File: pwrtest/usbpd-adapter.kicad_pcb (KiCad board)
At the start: 2 copper layers, 61.2 x 45.5 mm, 49 parts, among them J1 Conn_01x04, J2 Conn_01x04, J3 USB_C_Receptacle_USB2.0_16P, J5 Screw_Terminal_01x03, Q1 AO3400A, U1 AP63205WU, U2 L7812, U3 IP2721, U4 TPS5430DDA, U5 L7905

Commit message: adding undervoltage detection circuits
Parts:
- added D10: LED, Diode_SMD:D_0603_1608Metric_Pad1.05x0.95mm_HandSolder, F.Cu at (114.0, 39.2)
- added D11: LED, Diode_SMD:D_0603_1608Metric_Pad1.05x0.95mm_HandSolder, F.Cu at (114.0, 41.8)
- added D12: LED, Diode_SMD:D_0603_1608Metric_Pad1.05x0.95mm_HandSolder, F.Cu at (114.0, 44.4)
- added D8: LED, Diode_SMD:D_0603_1608Metric_Pad1.05x0.95mm_HandSolder, F.Cu at (114.0, 34.0)
- added D9: LED, Diode_SMD:D_0603_1608Metric_Pad1.05x0.95mm_HandSolder, F.Cu at (114.0, 36.6)
- added Q2: BC847, Package_TO_SOT_SMD:SOT-23, F.Cu at (91.4, 34.9)
- added Q3: BC847, Package_TO_SOT_SMD:SOT-23, F.Cu at (91.4, 39.4)
- added Q4: BC847, Package_TO_SOT_SMD:SOT-23, F.Cu at (91.4, 43.8)
- added Q5: BC847, Package_TO_SOT_SMD:SOT-23, F.Cu at (91.4, 48.3)
- added Q6: BC857, Package_TO_SOT_SMD:SOT-23, F.Cu at (91.4, 52.7)
- added R11: 36k, Resistor_SMD:R_0603_1608Metric_Pad0.98x0.95mm_HandSolder, F.Cu at (100.9, 34.0)
- added R14: 10k, Resistor_SMD:R_0603_1608Metric_Pad0.98x0.95mm_HandSolder, F.Cu at (100.9, 36.5)
- added R15: 10k, Resistor_SMD:R_0603_1608Metric_Pad0.98x0.95mm_HandSolder, F.Cu at (100.9, 39.0)
- added R16: 560, Resistor_SMD:R_0603_1608Metric_Pad0.98x0.95mm_HandSolder, F.Cu at (100.9, 41.5)
- added R17: 47k, Resistor_SMD:R_0603_1608Metric_Pad0.98x0.95mm_HandSolder, F.Cu at (100.9, 44.0)
- added R18: 10k, Resistor_SMD:R_0603_1608Metric_Pad0.98x0.95mm_HandSolder, F.Cu at (100.9, 46.5)
- added R19: 10k, Resistor_SMD:R_0603_1608Metric_Pad0.98x0.95mm_HandSolder, F.Cu at (100.9, 49.0)
- added R20: 560, Resistor_SMD:R_0603_1608Metric_Pad0.98x0.95mm_HandSolder, F.Cu at (100.9, 51.5)
- added R21: 8.2k, Resistor_SMD:R_0603_1608Metric_Pad0.98x0.95mm_HandSolder, F.Cu at (105.2, 34.0)
- added R22: 10k, Resistor_SMD:R_0603_1608Metric_Pad0.98x0.95mm_HandSolder, F.Cu at (105.2, 36.5)
- added R23: 10k, Resistor_SMD:R_0603_1608Metric_Pad0.98x0.95mm_HandSolder, F.Cu at (105.2, 39.0)
- added R24: 560, Resistor_SMD:R_0603_1608Metric_Pad0.98x0.95mm_HandSolder, F.Cu at (105.2, 41.5)
- added R25: 36k, Resistor_SMD:R_0603_1608Metric_Pad0.98x0.95mm_HandSolder, F.Cu at (105.2, 44.0)
- added R26: 10k, Resistor_SMD:R_0603_1608Metric_Pad0.98x0.95mm_HandSolder, F.Cu at (105.2, 46.5)
- added R27: 10k, Resistor_SMD:R_0603_1608Metric_Pad0.98x0.95mm_HandSolder, F.Cu at (105.2, 49.0)
- added R28: 560, Resistor_SMD:R_0603_1608Metric_Pad0.98x0.95mm_HandSolder, F.Cu at (105.2, 51.5)
- added R29: 10k, Resistor_SMD:R_0603_1608Metric_Pad0.98x0.95mm_HandSolder, F.Cu at (109.6, 34.0)
- added R30: 8.2k, Resistor_SMD:R_0603_1608Metric_Pad0.98x0.95mm_HandSolder, F.Cu at (109.6, 36.5)
- added R31: 10k, Resistor_SMD:R_0603_1608Metric_Pad0.98x0.95mm_HandSolder, F.Cu at (109.6, 39.0)
- added R32: 560, Resistor_SMD:R_0603_1608Metric_Pad0.98x0.95mm_HandSolder, F.Cu at (109.6, 41.5)
- added R33: 10k, Resistor_SMD:R_0603_1608Metric_Pad0.98x0.95mm_HandSolder, F.Cu at (109.6, 44.0)
- added R34: 10k, Resistor_SMD:R_0603_1608Metric_Pad0.98x0.95mm_HandSolder, F.Cu at (109.6, 46.5)
- added U10: TL431, Package_TO_SOT_SMD:SOT-23, F.Cu at (96.3, 52.7)
- added U6: TL431DBZ, Package_TO_SOT_SMD:SOT-23, F.Cu at (96.3, 34.9)
- added U7: TL431DBZ, Package_TO_SOT_SMD:SOT-23, F.Cu at (96.3, 39.4)
- added U8: TL431DBZ, Package_TO_SOT_SMD:SOT-23, F.Cu at (96.3, 43.8)
- added U9: TL431, Package_TO_SOT_SMD:SOT-23, F.Cu at (96.3, 48.3)
- R12: value 620 -> 390
- R13: value 2k -> 1.8k

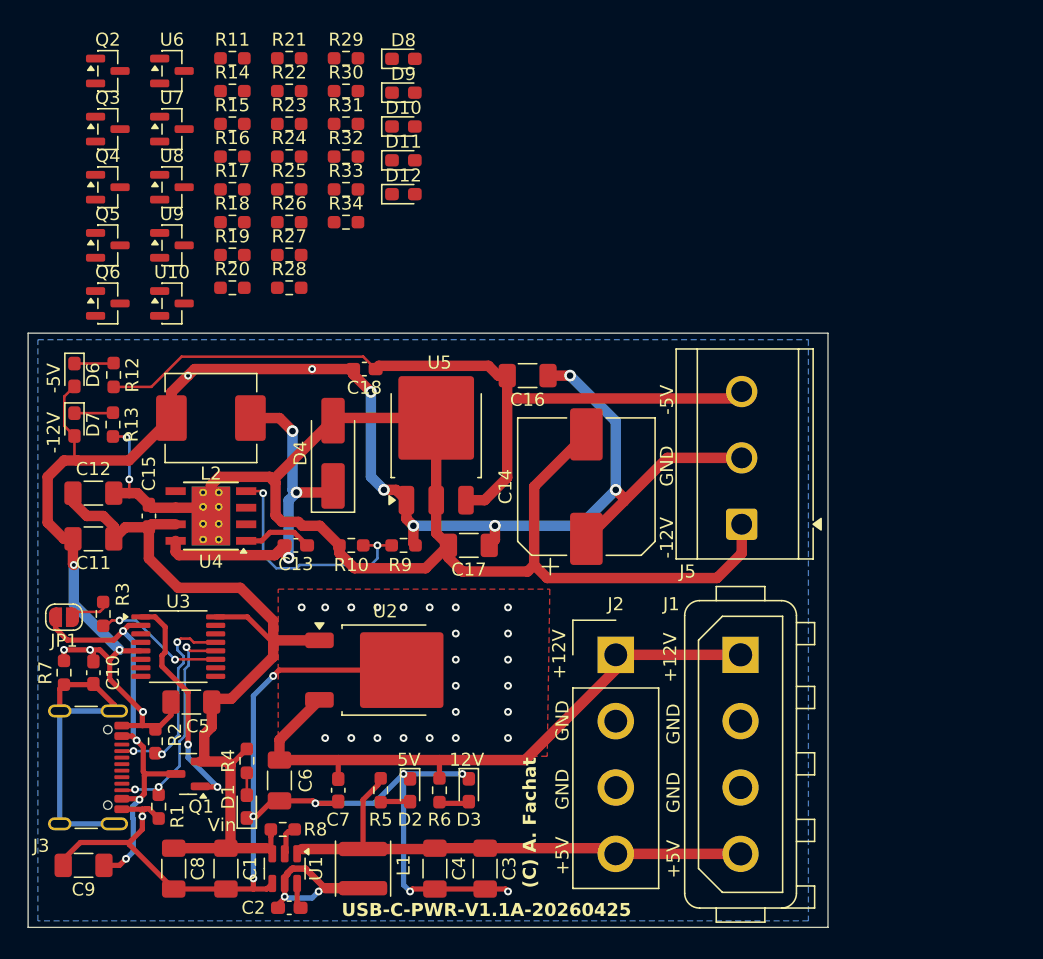
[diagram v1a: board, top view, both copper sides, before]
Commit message: new pwr adapter layout
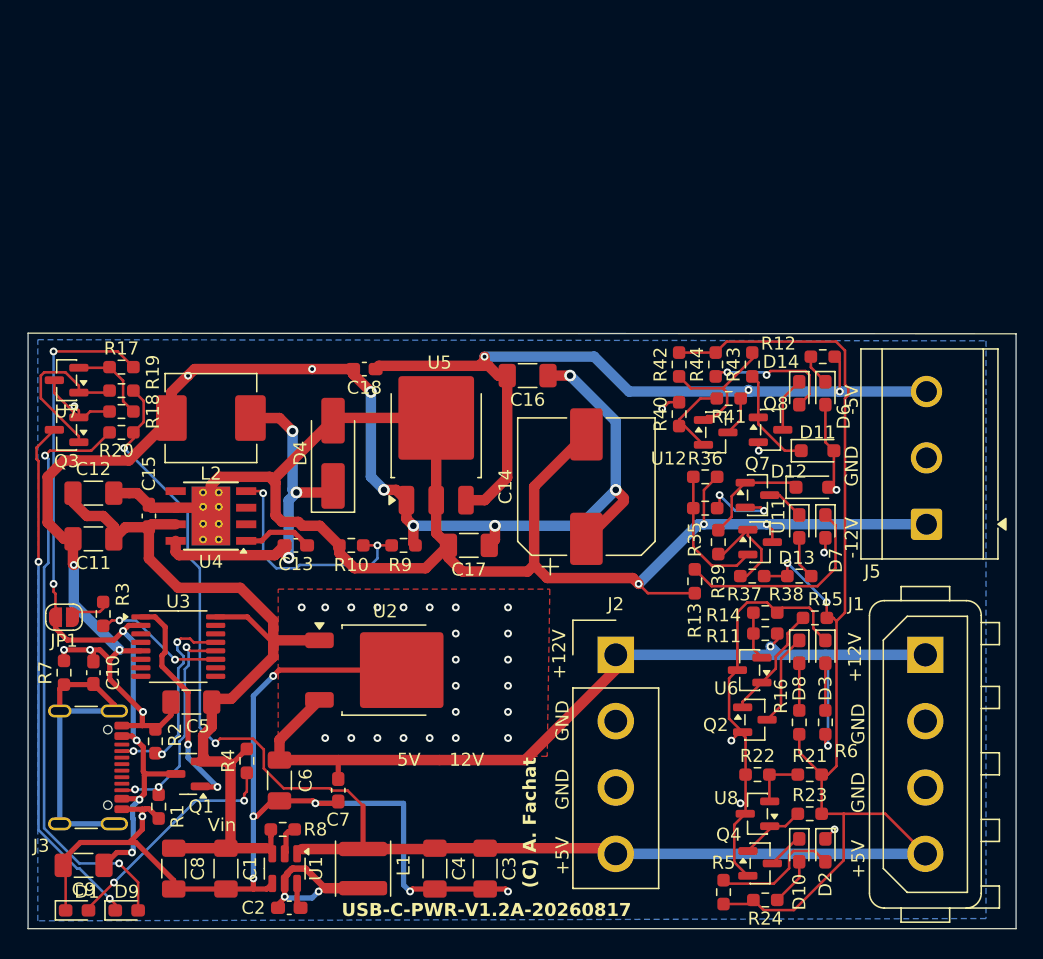
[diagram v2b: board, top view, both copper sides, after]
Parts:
- removed Q5: BC847, Package_TO_SOT_SMD:SOT-23
- removed Q6: BC857, Package_TO_SOT_SMD:SOT-23
- removed R25: 36k, Resistor_SMD:R_0603_1608Metric_Pad0.98x0.95mm_HandSolder
- removed R26, R27, R29, R31, R33, R34: 10k, Resistor_SMD:R_0603_1608Metric_Pad0.98x0.95mm_HandSolder
- removed R28, R32: 560, Resistor_SMD:R_0603_1608Metric_Pad0.98x0.95mm_HandSolder
- removed R30: 8.2k, Resistor_SMD:R_0603_1608Metric_Pad0.98x0.95mm_HandSolder
- removed U10, U9: TL431, Package_TO_SOT_SMD:SOT-23
- added D13: LED, Diode_SMD:D_0603_1608Metric_Pad1.05x0.95mm_HandSolder, F.Cu at (144.3, 69.8)
- added D14: LED, Diode_SMD:D_0603_1608Metric_Pad1.05x0.95mm_HandSolder, F.Cu at (144.3, 59.6)
- added Q7: BC847, Package_TO_SOT_SMD:SOT-23, F.Cu at (141.1, 67.4)
- added Q8: BC847, Package_TO_SOT_SMD:SOT-23, F.Cu at (142.1, 62.4)
- added R35: 36k, Resistor_SMD:R_0603_1608Metric_Pad0.98x0.95mm_HandSolder, F.Cu at (137.1, 68.4)
- added R36: 10k, Resistor_SMD:R_0603_1608Metric_Pad0.98x0.95mm_HandSolder, F.Cu at (137.1, 66.0)
- added R37: 2.2k, Resistor_SMD:R_0603_1608Metric_Pad0.98x0.95mm_HandSolder, F.Cu at (140.7, 73.6)
- added R38: 560, Resistor_SMD:R_0603_1608Metric_Pad0.98x0.95mm_HandSolder, F.Cu at (144.3, 73.6)
- added R39: 10k, Resistor_SMD:R_0603_1608Metric_Pad0.98x0.95mm_HandSolder, F.Cu at (138.1, 71.0)
- added R40: 8.6k, Resistor_SMD:R_0603_1608Metric_Pad0.98x0.95mm_HandSolder, F.Cu at (135.1, 61.2)
- added R41: 10k, Resistor_SMD:R_0603_1608Metric_Pad0.98x0.95mm_HandSolder, F.Cu at (138.9, 60.0)
- added R42: 2.2k, Resistor_SMD:R_0603_1608Metric_Pad0.98x0.95mm_HandSolder, F.Cu at (135.1, 57.4)
- added R43: 10k, Resistor_SMD:R_0603_1608Metric_Pad0.98x0.95mm_HandSolder, F.Cu at (140.7, 57.4)
- added R44: 560, Resistor_SMD:R_0603_1608Metric_Pad0.98x0.95mm_HandSolder, F.Cu at (137.9, 57.4)
- added U11: TL431, Package_TO_SOT_SMD:SOT-23, F.Cu at (141.3, 71.0)
- added U12: TL431, Package_TO_SOT_SMD:SOT-23, F.Cu at (137.9, 62.6)
- D11, D12: value LED -> 1N4148; footprint Diode_SMD:D_0603_1608Metric_Pad1.05x0.95mm_HandSolder -> Diode_SMD:D_SOD-323_HandSoldering
- moved Q4 71.9 mm to (141.3, 95.6)
- moved Q2 70.2 mm to (140.9, 84.6)
- moved R21 67.8 mm to (145.1, 88.8)
- moved R24 67.6 mm to (141.7, 98.4), turned to 180 degrees
- moved R23 66.2 mm to (145.1, 91.8)
- moved D9 66.1 mm to (92.8, 99.2)
- moved U8 65.7 mm to (141.1, 91.8), turned to 180 degrees
- moved U6 63.7 mm to (140.5, 80.8), turned to 180 degrees
- moved R22 63.4 mm to (141.1, 88.8)
- moved D10 63.2 mm to (144.3, 94.6), turned to -90 degrees
- moved R16 61.3 mm to (144.3, 84.8), turned to -90 degrees
- moved R11 60.0 mm to (141.7, 78.0)
- moved R15 58.5 mm to (145.5, 76.8)
- moved D7 58.0 mm to (146.3, 69.8)
- moved D6 57.5 mm to (146.3, 59.6)
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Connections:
- D11 pad 1: -5V -> Net-(D11-K)
- D11 pad 2: Net-(D11-A) -> GND
- D12 pad 2: Net-(D12-A) -> GND
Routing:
- net 5V: track 40.3 -> 183.9 mm, vias 0 -> 4
- net Net-(D9-A): track 0.00 -> 45.5 mm, vias 0 -> 2
- net Net-(D9-K): track 0.00 -> 40.0 mm, vias 0 -> 2
- net GND: track 221.5 -> 257.2 mm, vias 45 -> 53
- net VBUS: track 33.8 -> 60.8 mm, vias 4 -> 6
- net 12V: track 48.0 -> 70.9 mm, vias 0 -> 2
- net -12V: track 103.6 -> 121.6 mm, vias 2 -> 3
- net Net-(D1-A): track 1.43 -> 17.7 mm, vias 0 -> 2
- net Net-(D7-K): track 2.97 -> 16.3 mm
- net Net-(Q3-B): track 0.00 -> 12.7 mm
- net Net-(U12-K): track 0.00 -> 11.1 mm
- net Net-(U11-REF): track 0.00 -> 10.5 mm
- net Net-(D14-A): track 0.00 -> 10.2 mm, vias 0 -> 2
- net Net-(Q2-B): track 0.00 -> 8.77 mm
- net Net-(D12-K): track 0.00 -> 8.52 mm
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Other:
- board size 61.2 x 45.5 mm -> 75.7 x 45.6 mm
- board text added: "USB-C-PWR-V1.2A-20260817"
- board text removed: "USB-C-PWR-V1.1A-20260425"

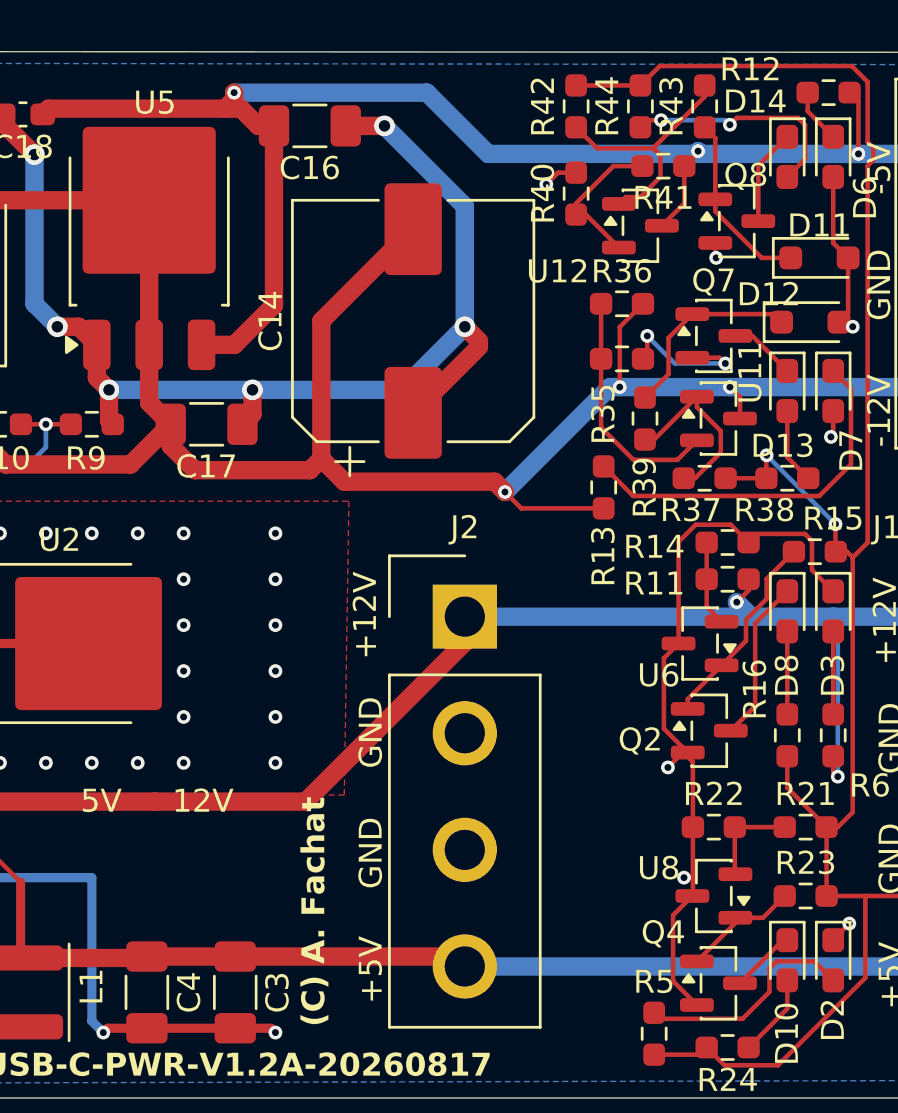
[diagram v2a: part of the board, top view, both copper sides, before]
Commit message: add 0V in main pwr outputs
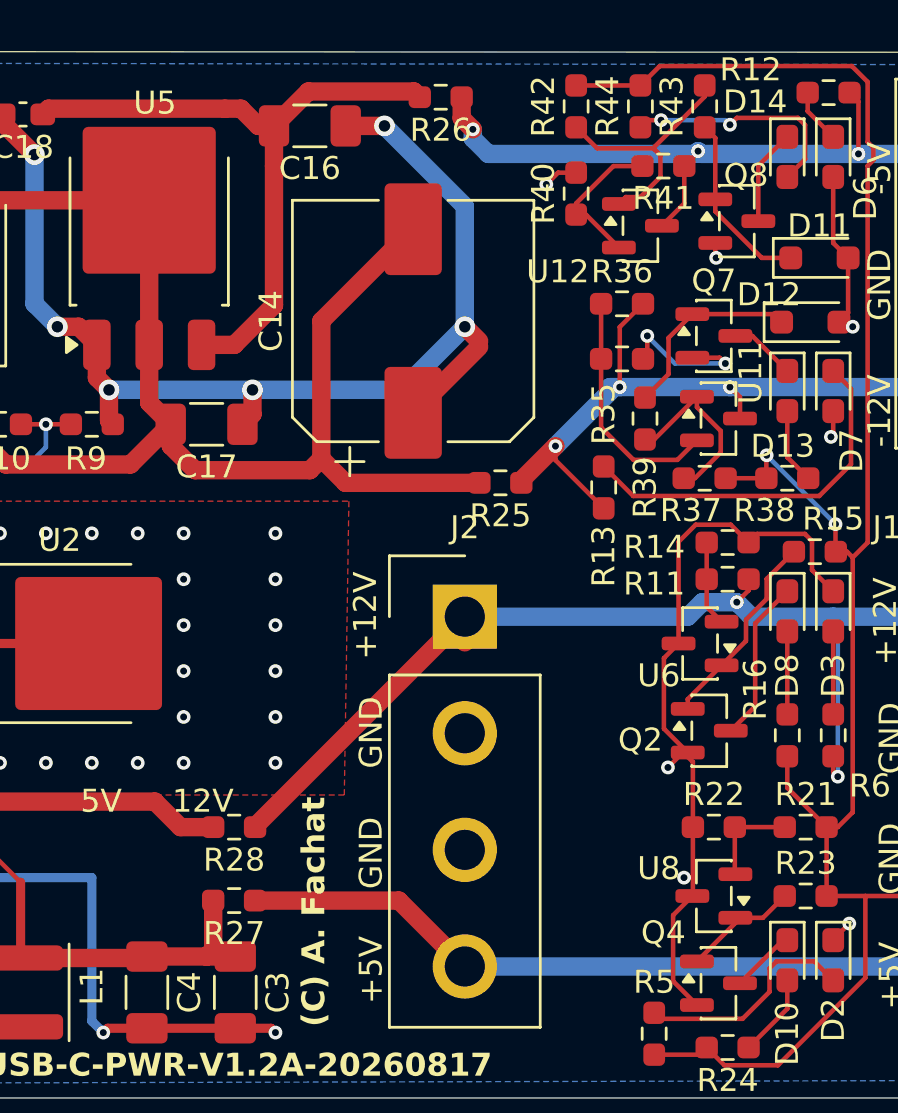
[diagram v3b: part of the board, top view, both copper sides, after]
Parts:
- added R25: 0, Resistor_SMD:R_0603_1608Metric_Pad0.98x0.95mm_HandSolder, F.Cu at (131.8, 73.8)
- added R26: 0, Resistor_SMD:R_0603_1608Metric_Pad0.98x0.95mm_HandSolder, F.Cu at (129.2, 57.0)
- added R27: 0, Resistor_SMD:R_0603_1608Metric_Pad0.98x0.95mm_HandSolder, F.Cu at (120.2, 92.0)
- added R28: 0, Resistor_SMD:R_0603_1608Metric_Pad0.98x0.95mm_HandSolder, F.Cu at (120.2, 88.8)
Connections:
- C12 pad 2: -12V -> /Negative Voltages/-12VP
- C14 pad 2: -12V -> /Negative Voltages/-12VP
- C15 pad 2: -12V -> /Negative Voltages/-12VP
- C16 pad 2: -5V -> Net-(U5-VO)
- C17 pad 2: -12V -> /Negative Voltages/-12VP
- C18 pad 1: -5V -> Net-(U5-VO)
- C3 pad 1: 5V -> 5VP
- C4 pad 1: 5V -> 5VP
- C6 pad 1: 12V -> /Positive Voltages/12VPP
- C7 pad 2: 12V -> /Positive Voltages/12VPP
- D4 pad 2: -12V -> /Negative Voltages/-12VP
- L1 pad 2: 5V -> 5VP
- R10 pad 1: -12V -> /Negative Voltages/-12VP
- R19 pad 2: 5V -> 5VP
- R20 pad 2: 5V -> 5VP
- U1 pad 1: 5V -> 5VP
- U2 pad 3: 12V -> /Positive Voltages/12VPP
- U4 pad 6: -12V -> /Negative Voltages/-12VP
- U4 pad 9: -12V -> /Negative Voltages/-12VP
- U5 pad 2: -12V -> /Negative Voltages/-12VP
- U5 pad 3: -5V -> Net-(U5-VO)
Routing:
- net -12V: track 121.6 -> 32.4 mm
- net /Negative Voltages/-12VP: track 0.00 -> 86.1 mm
- net 5VP: track 0.00 -> 65.7 mm, vias 0 -> 2
- net 5V: track 183.9 -> 121.6 mm, vias 4 -> 2
- net -5V: track 65.6 -> 33.3 mm
- net Net-(U5-VO): track 0.00 -> 29.2 mm
- net 12V: track 70.9 -> 47.5 mm
- net /Positive Voltages/12VPP: track 0.00 -> 22.6 mm

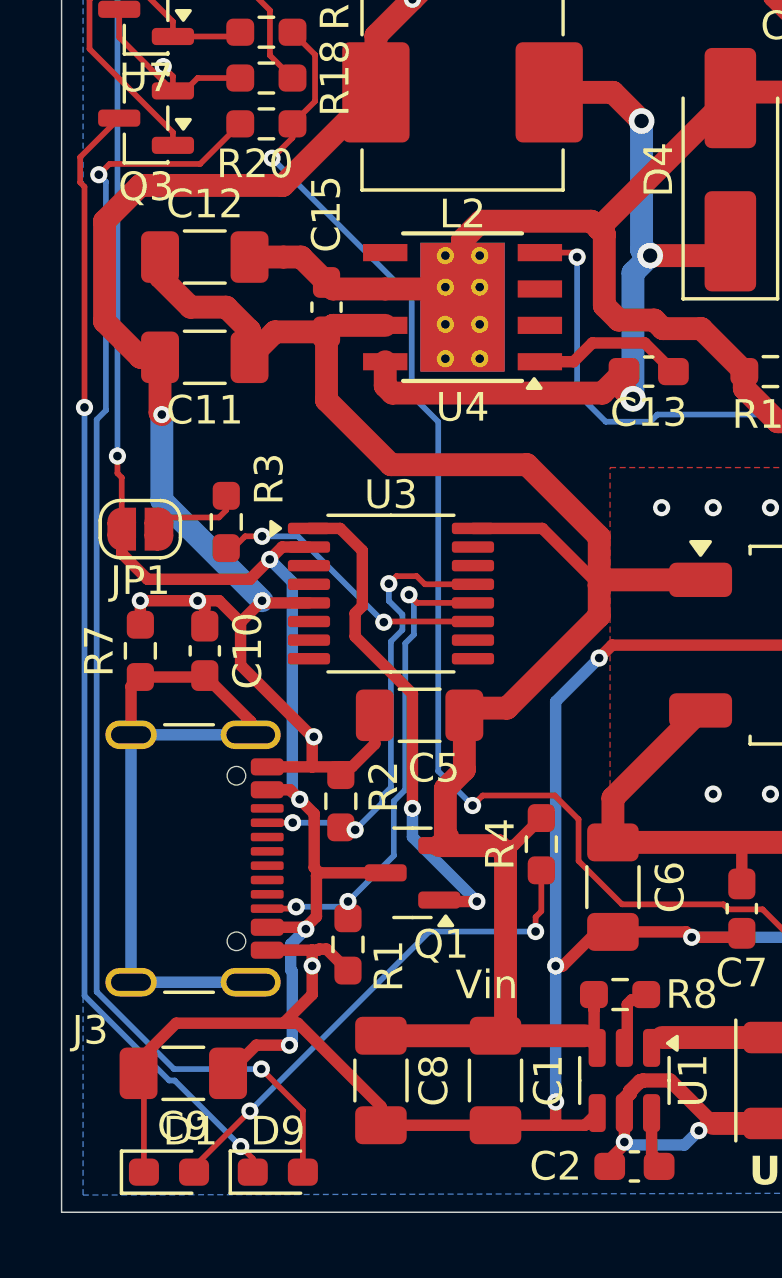
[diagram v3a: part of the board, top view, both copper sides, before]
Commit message: new usb controller
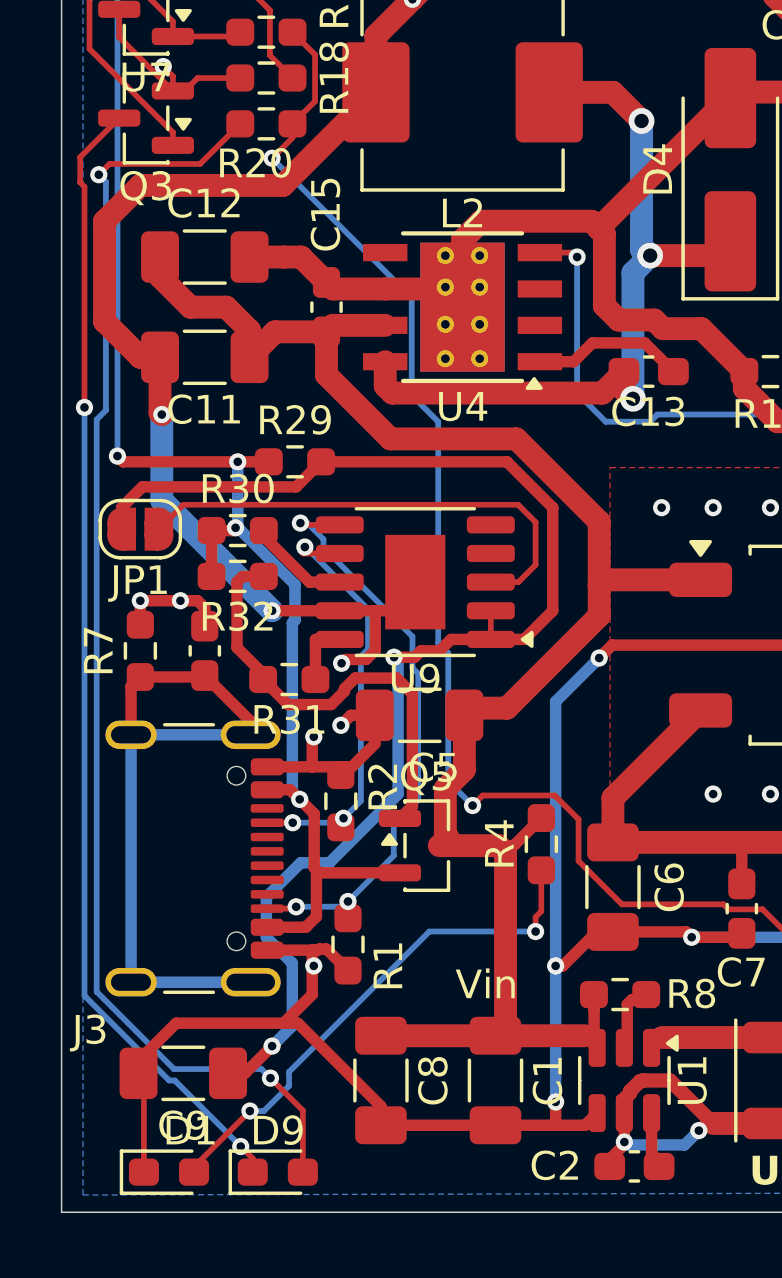
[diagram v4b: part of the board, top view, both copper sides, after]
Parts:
- removed Q1: AO3400A, Package_TO_SOT_SMD:SOT-23
- removed R3: 100k, Resistor_SMD:R_0603_1608Metric_Pad0.98x0.95mm_HandSolder
- removed U3: IP2721, Package_SO:TSSOP-16_4.4x5mm_P0.65mm
- added Q5: DMP3099L, Package_TO_SOT_SMD:SOT-23, F.Cu at (98.0, 87.8)
- added R29: 1k, Resistor_SMD:R_0603_1608Metric_Pad0.98x0.95mm_HandSolder, F.Cu at (93.4, 74.4)
- added R30: 10k, Resistor_SMD:R_0603_1608Metric_Pad0.98x0.95mm_HandSolder, F.Cu at (91.4, 76.8)
- added R31: 10k, Resistor_SMD:R_0603_1608Metric_Pad0.98x0.95mm_HandSolder, F.Cu at (93.2, 82.0)
- added R32: 10k, Resistor_SMD:R_0603_1608Metric_Pad0.98x0.95mm_HandSolder, F.Cu at (91.4, 78.4)
- added U9: CH224K, Package_SO:SSOP-10-1EP_3.9x4.9mm_P1mm_EP2.1x3.3mm, F.Cu at (97.6, 78.6)
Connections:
- C9 pad 1: VBUS -> Net-(JP1-B)
- JP1 pad 2: VBUS -> Net-(JP1-B)
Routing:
- net Net-(JP1-B): track 0.00 -> 46.7 mm, vias 0 -> 2
- net Net-(Q1-G): track 17.6 -> 0.00 mm, vias 2 -> 0
- net Net-(Q5-G): track 0.00 -> 15.6 mm
- net Net-(JP1-A): track 3.12 -> 17.1 mm
- net Net-(U3-SEL): track 10.0 -> 0.00 mm, vias 2 -> 0
- net VBUS: track 60.8 -> 55.4 mm, vias 6 -> 5
- net VIN: track 67.8 -> 62.9 mm
- net Net-(U9-VBUS): track 0.00 -> 3.52 mm
- net Net-(J3-CC2): track 17.6 -> 21.0 mm
- net Net-(U9-PG): track 0.00 -> 2.24 mm
- net Net-(J3-CC1): track 16.3 -> 15.5 mm
- net GND: track 257.2 -> 257.7 mm, vias 53 -> 55
